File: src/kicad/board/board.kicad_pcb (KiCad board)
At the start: 2 copper layers, 100.5 x 70.6 mm, 82 parts, among them J1 USB_C_Receptacle_USB2.0, J2 Conn_01x06, J3 Micro_SD_Card_Det, J4 Conn_01x05_Male, J5 Conn_01x05_Male, J6 PWR_EN, J7 Screw_Terminal_Speaker, Q1 DMG2305UX, SW1 SW_Keyboard, SW2 SW_Keyboard, SW3 RotEncoder_S, SW4 SW_Keyboard, SW5 SW_Keyboard, SW6 BOOTSEL, U1 MCP23017_ML, U2 BQ25172, U3 TLV61070A, U4 XC6206P332MR, U5 MAX98357, U6 RP2040, U7 W25Q128JVS, Y1 X322512MSB4SI

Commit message: update
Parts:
- moved C12 22.2 mm to (170.3, 34.7)
- moved C13 22.2 mm to (174.7, 31.7)
- moved FB1 22.2 mm to (170.5, 32.0)
- moved FB2 22.2 mm to (166.5, 37.4)
- moved C11 22.2 mm to (170.2, 38.2)
- moved U5 22.2 mm to (165.6, 33.3)
- moved C10 14.3 mm to (173.4, 36.4)
- moved C8 6.80 mm to (151.4, 66.1)
- moved C9 2.35 mm to (155.3, 63.5), turned to -90 degrees
- moved U4 1.74 mm to (152.6, 63.4), turned to 180 degrees
- moved D5 1.03 mm to (147.7, 67.2)
- moved R13 0.51 mm to (147.1, 64.8)
- moved R17 0.38 mm to (142.9, 67.0)
- moved R20 0.24 mm to (123.5, 77.8)
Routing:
- net /Power/BAT_OR_USB_POWER: track 0.00 -> 41.9 mm, vias 0 -> 4
- net GND: track 39.0 -> 73.6 mm, vias 21 -> 30
- net Net-(C4-Pad1): track 3.81 -> 34.8 mm
- net VDD: track 0.00 -> 16.5 mm
- net Net-(BT1-Pad1): track 52.3 -> 68.1 mm, vias 1 -> 3
- net Net-(D5-Pad1): track 0.00 -> 7.43 mm
- net Net-(L1-Pad2): track 0.00 -> 6.52 mm
- net Net-(R16-Pad1): track 0.00 -> 5.52 mm, vias 0 -> 2
- net Net-(R12-Pad2): track 0.00 -> 4.61 mm
- net +3.3V: track 18.5 -> 22.5 mm, vias 0 -> 2
- net Net-(R14-Pad2): track 0.00 -> 3.92 mm
- net Net-(R17-Pad1): track 0.00 -> 3.13 mm
- net Net-(R11-Pad2): track 0.00 -> 2.71 mm
- net Net-(D5-Pad2): track 0.00 -> 2.63 mm

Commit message: update
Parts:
- removed FB1, FB2: Ferrite, Library:Ferrite-0805
- removed J2: Conn_01x06, Connector_PinHeader_2.54mm:PinHeader_1x06_P2.54mm_Vertical
- moved C13 35.6 mm to (167.2, 66.5), turned to -90 degrees
- moved C10 32.4 mm to (159.2, 65.5), turned to 90 degrees
- moved C12 32.1 mm to (165.5, 66.5), turned to 90 degrees
- moved U5 30.9 mm to (162.2, 64.0)
- moved C11 29.7 mm to (158.0, 65.2), turned to 90 degrees
- moved R4 7.74 mm to (122.0, 54.6), turned to -90 degrees
- moved R8 6.84 mm to (114.5, 50.5), turned to -90 degrees
- moved R7 5.41 mm to (120.5, 53.8), turned to -90 degrees
- moved R5 4.69 mm to (119.0, 53.1), turned to 90 degrees
- moved SW6 4.19 mm to (128.8, 53.0), turned to 0 degrees
- moved R3 4.08 mm to (116.0, 51.6), turned to -90 degrees
- moved C2 3.05 mm to (112.0, 56.7)
- moved C1 2.85 mm to (112.0, 50.2), turned to -90 degrees
- moved R6 2.76 mm to (117.5, 52.3), turned to -90 degrees
- moved C23 0.78 mm to (117.3, 61.5)
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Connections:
- U5 pad 10: Net-(FB2-Pad1) -> Net-(C13-Pad2)
- U5 pad 9: Net-(FB1-Pad1) -> Net-(C12-Pad1)
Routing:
- net AMP_LRCLK: track 0.00 -> 43.8 mm, vias 0 -> 2
- net AMP_DIN: track 0.00 -> 41.6 mm
- net AMP_BCLK: track 0.00 -> 40.3 mm, vias 0 -> 2
- net Net-(C13-Pad2): track 0.00 -> 38.5 mm
- net Net-(C12-Pad1): track 0.00 -> 37.5 mm
- net SD_MISO: track 0.00 -> 34.0 mm, vias 0 -> 2
- net SD_DAT2: track 0.00 -> 32.1 mm
- net SD_CS: track 0.00 -> 31.3 mm, vias 0 -> 2
- net SD_DAT1: track 0.00 -> 30.8 mm, vias 0 -> 2
- net SD_CLK: track 0.00 -> 30.6 mm, vias 0 -> 2
- net SD_MOSI: track 0.00 -> 30.0 mm, vias 0 -> 2
- net GND: track 73.6 -> 85.6 mm, vias 30 -> 49
- net VDD: track 16.5 -> 26.5 mm
- net /rp2040/QSPI_SD2: track 9.39 -> 10.7 mm
- net RP2040_SCL: track 40.9 -> 41.6 mm
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
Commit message: update
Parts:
- moved H1 93.2 mm to (101.2, 100.2)
- moved H2 92.6 mm to (194.2, 113.7)
- moved SW3 88.1 mm to (186.8, 107.4), turned to 90 degrees
- moved U1 46.5 mm to (168.3, 112.0)
- moved C3 35.3 mm to (164.0, 113.2), turned to -90 degrees
- moved SW5 32.2 mm to (112.9, 100.2)
- moved J5 13.9 mm to (153.4, 107.6), turned to 180 degrees
- moved SW2 12.3 mm to (151.2, 100.2)
- moved C11 10.8 mm to (156.7, 76.0), turned to 180 degrees
- moved C10 10.5 mm to (159.4, 76.0), turned to 0 degrees
- moved SW1 10.3 mm to (170.4, 100.2)
- moved U5 9.50 mm to (158.3, 72.6)
- moved C13 5.72 mm to (161.6, 65.6)
- moved SW4 5.44 mm to (132.0, 100.2)
- moved R9 4.36 mm to (109.1, 65.8)
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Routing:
- net B3: track 0.00 -> 66.8 mm
- net B2: track 0.00 -> 50.5 mm
- net B6: track 0.00 -> 47.8 mm, vias 0 -> 1
- net B1: track 0.00 -> 33.9 mm
- net B5: track 0.00 -> 32.6 mm, vias 0 -> 1
- net /Input/INT: track 0.00 -> 28.2 mm
- net /Input/GND_LOCAL: track 0.00 -> 26.9 mm, vias 0 -> 8
- net B4: track 0.00 -> 25.1 mm, vias 0 -> 1
- net /Input/SDA: track 0.00 -> 22.0 mm, vias 0 -> 2
- net /Input/SCK: track 0.00 -> 21.5 mm, vias 0 -> 2
- net VDD: track 26.5 -> 47.3 mm
- net B0: track 0.00 -> 15.7 mm
- net +1V1: track 6.46 -> 17.5 mm
- net Net-(C13-Pad2): track 38.5 -> 49.1 mm
- net /USB_D-: track 0.00 -> 8.17 mm
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- added copper zone on F.Cu, net /Input/3.3V_LOCAL
- added copper zone on B.Cu, net /Input/GND_LOCAL
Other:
- board size 100.5 x 70.6 mm -> 100.2 x 70.6 mm
- board text added: "FOREVER WIP V0.2"

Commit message: update
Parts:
- R17: value 20K -> 27K
- moved J6 4.32 mm to (173.3, 78.5), turned to -90 degrees
- moved R8 2.70 mm to (115.3, 53.1)
- moved R6 1.87 mm to (118.5, 53.9)
- moved R3 1.75 mm to (116.8, 53.1)
- moved R7 1.39 mm to (121.6, 54.7)
- moved R5 1.32 mm to (120.0, 53.9)
- moved C12 1.18 mm to (164.3, 66.0)
- moved R4 1.15 mm to (123.1, 54.7)
- moved C1 0.99 mm to (113.0, 50.9)
- moved C2 0.85 mm to (112.8, 57.1)
- moved J3 0.66 mm to (105.5, 54.3)
- moved C13 0.61 mm to (162.1, 66.0)
- moved C8 0.61 mm to (151.9, 66.5)
- moved C9 0.61 mm to (156.1, 63.8)
- moved H4 0.61 mm to (194.5, 64.0)
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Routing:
- net Net-(C12-Pad1): track 43.5 -> 49.8 mm
- net VDD: track 47.3 -> 42.3 mm
- net /Power/BAT_OR_USB_POWER: track 45.9 -> 49.8 mm
- net GND: track 88.6 -> 90.9 mm
- net SD_DAT2: track 32.1 -> 29.8 mm
- net SD_MISO: track 34.0 -> 35.7 mm
- net /rp2040/QSPI_SS: track 25.8 -> 24.9 mm
- net SD_CS: track 31.3 -> 30.5 mm
- net +3.3V: track 30.1 -> 29.3 mm
- net SD_DAT1: track 30.8 -> 30.2 mm
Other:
- board size 100.2 x 70.6 mm -> 100 x 70 mm

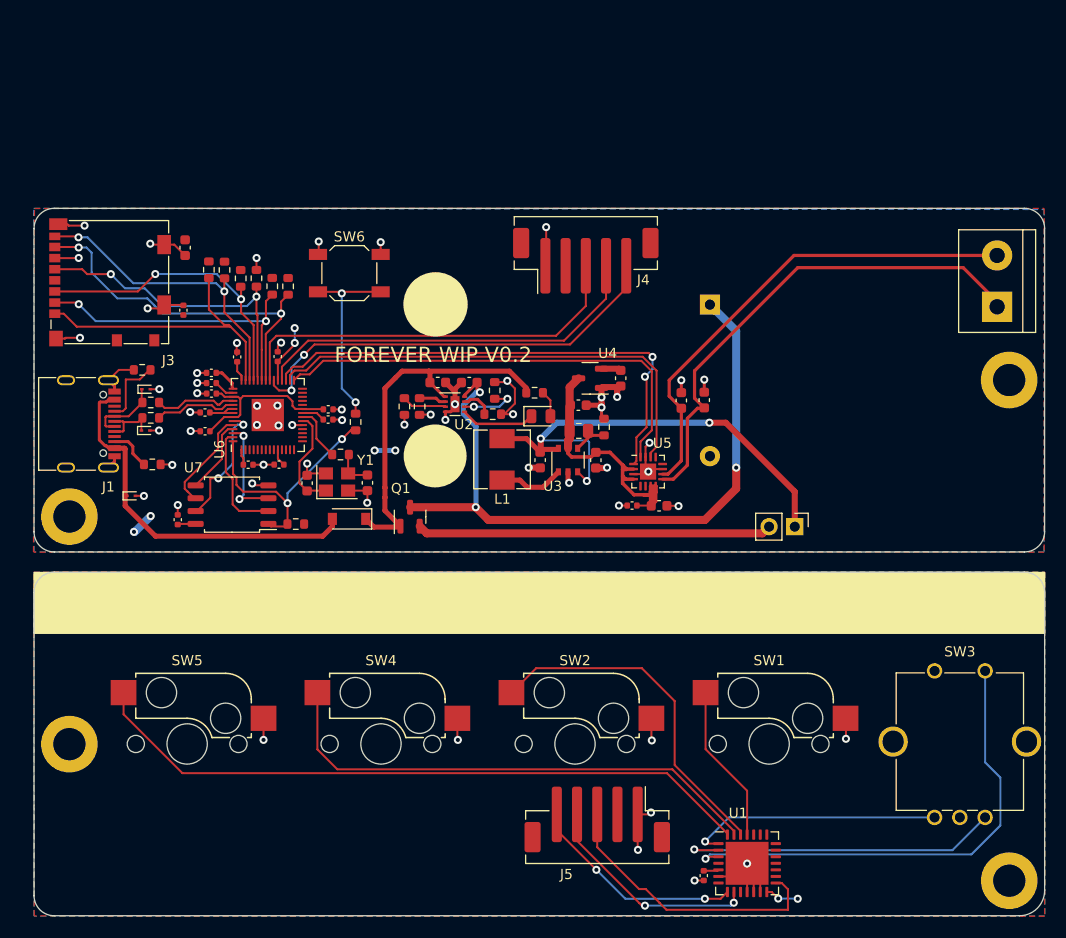
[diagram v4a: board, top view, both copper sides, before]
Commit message: separate io board from main
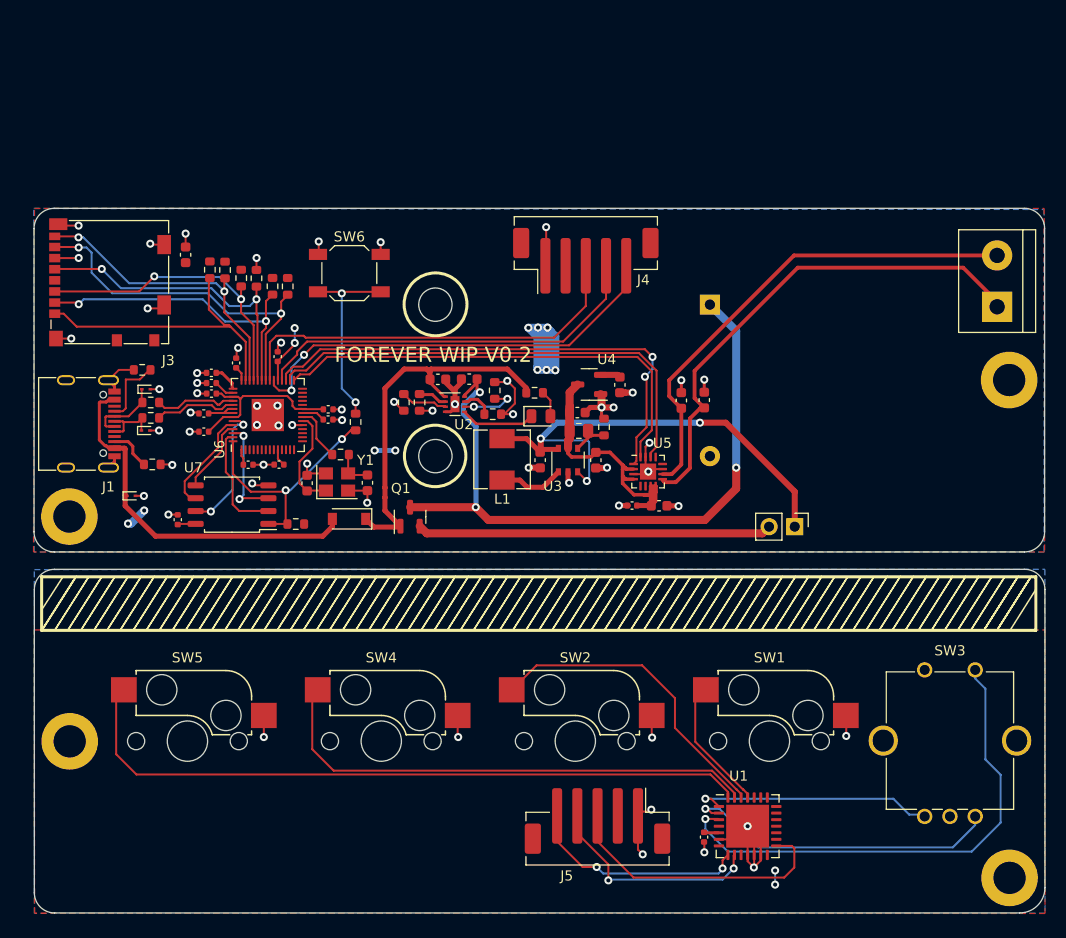
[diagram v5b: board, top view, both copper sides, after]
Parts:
- removed C2: 100nF, Capacitor_SMD:C_0402_1005Metric
- moved C3 3.81 mm to (164.3, 109.2)
- moved U1 3.67 mm to (168.6, 108.1)
- moved SW3 0.99 mm to (186.1, 107.2)
- moved C8 0.74 mm to (151.8, 67.2)
- moved C1 0.71 mm to (113.0, 51.6), turned to 90 degrees
- moved C9 0.66 mm to (156.0, 64.5)
- moved U4 0.62 mm to (152.9, 64.4)
- moved C23 0.61 mm to (118.0, 62.3)
- moved R12 0.41 mm to (134.6, 66.2)
- moved R11 0.41 mm to (136.2, 66.2)
- moved C7 0.34 mm to (141.1, 63.9)
- moved C4 0.31 mm to (138.0, 63.9)
- moved H1 0.28 mm to (101.5, 99.7)
- moved H2 0.28 mm to (194.5, 113.2)
- moved SW1 0.28 mm to (170.8, 99.7)
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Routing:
- net +3.3V: track 29.3 -> 54.9 mm, vias 6 -> 12
- net GND: track 90.9 -> 85.0 mm
- net /Input/GND_LOCAL: track 26.9 -> 32.6 mm, vias 8 -> 9
- net B1: track 34.4 -> 31.1 mm
- net B0: track 15.7 -> 13.2 mm
- net B3: track 66.8 -> 69.3 mm
- net B6: track 47.8 -> 50.0 mm
- net /Input/3.3V_LOCAL: track 4.83 -> 2.90 mm
- net B4: track 25.1 -> 24.0 mm
- net /rp2040/QSPI_SS: track 24.9 -> 23.9 mm
- net /Input/SCK: track 21.5 -> 22.5 mm
- net B5: track 32.6 -> 31.7 mm
- net VDD: track 42.3 -> 41.8 mm
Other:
- board size 100 x 70 mm -> 100 x 69.7 mm

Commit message: remove io-board stuff from the main board project
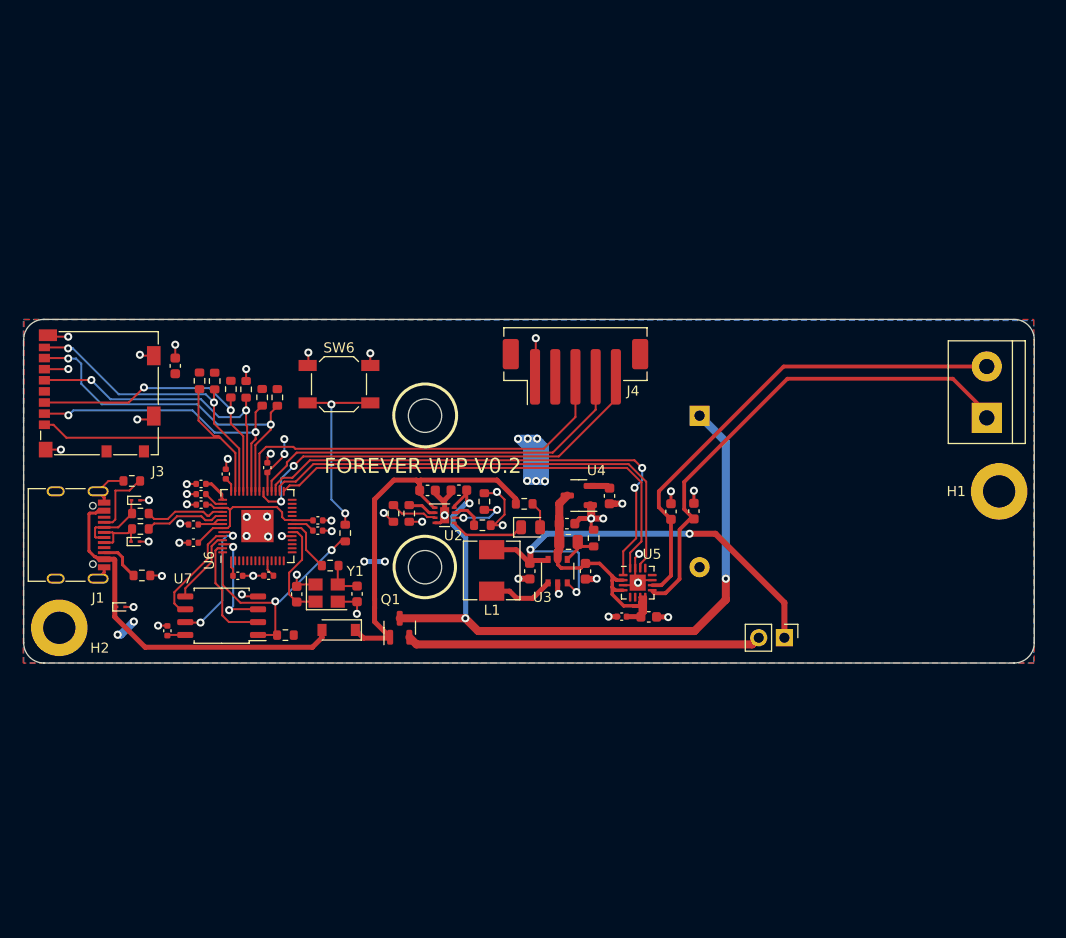
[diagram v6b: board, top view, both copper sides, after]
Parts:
- removed C3: 100nF, Capacitor_SMD:C_0402_1005Metric
- removed H3, H4: MountingHole, MountingHole:MountingHole_3.2mm_M3_DIN965_Pad
- removed J5: Conn_01x05_Male, Connector_JST:JST_PH_B5B-PH-SM4-TB_1x05-1MP_P2.00mm_Vertical
- removed SW1, SW2, SW4, SW5: SW_Keyboard, Library:Kailh_socket_MX
- removed SW3: RotEncoder_S, Rotary_Encoder:RotaryEncoder_Bourns_Vertical_PEC12R-3xxxF-Sxxxx
- removed U1: MCP23017_ML, Package_DFN_QFN:QFN-28-1EP_6x6mm_P0.65mm_EP4.25x4.25mm
- moved H2 97.2 mm to (100.5, 88.5)
- moved H1 95.2 mm to (193.5, 75.0)
- moved C11 11.0 mm to (156.2, 87.4)
- moved C15 11.0 mm to (130.0, 85.2)
- moved C23 11.0 mm to (117.0, 73.3)
- moved C5 11.0 mm to (147.1, 82.9)
- moved D5 11.0 mm to (147.1, 78.6)
- moved R14 11.0 mm to (150.9, 80.0)
- moved R16 11.0 mm to (142.6, 76.0)
- moved R20 11.0 mm to (122.9, 89.2)
- moved U2 11.0 mm to (138.6, 77.4)
- moved U3 11.0 mm to (149.8, 82.9)
- moved U7 11.0 mm to (116.6, 87.3)
- moved C14 11.0 mm to (124.0, 85.2)
- moved C17 11.0 mm to (113.8, 80.1)
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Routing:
- net B3: track 69.3 -> 0.00 mm
- net B2: track 50.1 -> 0.00 mm
- net B6: track 50.0 -> 0.00 mm, vias 1 -> 0
- net /Input/GND_LOCAL: track 32.6 -> 0.00 mm, vias 9 -> 0
- net B5: track 31.7 -> 0.00 mm, vias 1 -> 0
- net B1: track 31.1 -> 0.00 mm
- net /Input/INT: track 28.1 -> 0.00 mm
- net B4: track 24.0 -> 0.00 mm, vias 1 -> 0
- net /Input/SCK: track 22.5 -> 0.00 mm, vias 2 -> 0
- net /Input/SDA: track 22.3 -> 0.00 mm, vias 2 -> 0
- net B0: track 13.2 -> 0.00 mm
- net /Input/3.3V_LOCAL: track 2.90 -> 0.00 mm, vias 2 -> 0
- removed copper zone on F.Cu, net /Input/3.3V_LOCAL
- removed copper zone on B.Cu, net /Input/GND_LOCAL
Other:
- board size 100 x 69.7 mm -> 100 x 34 mm

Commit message: update
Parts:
- J6: value PWR_EN -> Conn_02x02_Top_Bottom; footprint Connector_PinHeader_2.54mm:PinHeader_1x02_P2.54mm_Vertical -> Connector_PinHeader_2.54mm:PinHeader_2x02_P2.54mm_Vertical
- moved J6 3.60 mm to (169.7, 86.9), turned to 0 degrees
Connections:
- C5 pad 1: /Power/BAT_OR_USB_POWER -> /Power/BAT_OR_USB_POWER_IN
- J6 pad 1: /Power/BAT_OR_USB_POWER -> /rp2040/SWCLK
- J6 pad 2: Net-(J6-Pad2) -> /rp2040/SWD
- L1 pad 1: /Power/BAT_OR_USB_POWER -> /Power/BAT_OR_USB_POWER_IN
- Q1 pad 2: Net-(J6-Pad2) -> /Power/BAT_OR_USB_POWER_OUT
- U3 pad 3: /Power/BAT_OR_USB_POWER -> /Power/BAT_OR_USB_POWER_IN
- U3 pad 6: /Power/BAT_OR_USB_POWER -> /Power/BAT_OR_USB_POWER_IN
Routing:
- net /rp2040/SWD: track 0.00 -> 59.2 mm, vias 0 -> 1
- net /rp2040/SWCLK: track 0.00 -> 56.7 mm, vias 0 -> 1
- net /Power/BAT_OR_USB_POWER_IN: track 0.00 -> 53.1 mm, vias 0 -> 3
- net /Power/BAT_OR_USB_POWER: track 49.8 -> 0.00 mm, vias 3 -> 0
- net Net-(J6-Pad2): track 35.1 -> 0.00 mm
- net /Power/BAT_OR_USB_POWER_OUT: track 0.00 -> 35.1 mm
- net +3.3V: track 54.9 -> 44.6 mm, vias 12 -> 10
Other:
- board text added: "POWER_EN"
- board text added: "SWCLK,SWD"
